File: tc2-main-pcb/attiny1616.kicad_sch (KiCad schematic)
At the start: 21 parts, among them SW101 SW_Push, U117 ATtiny1616-M

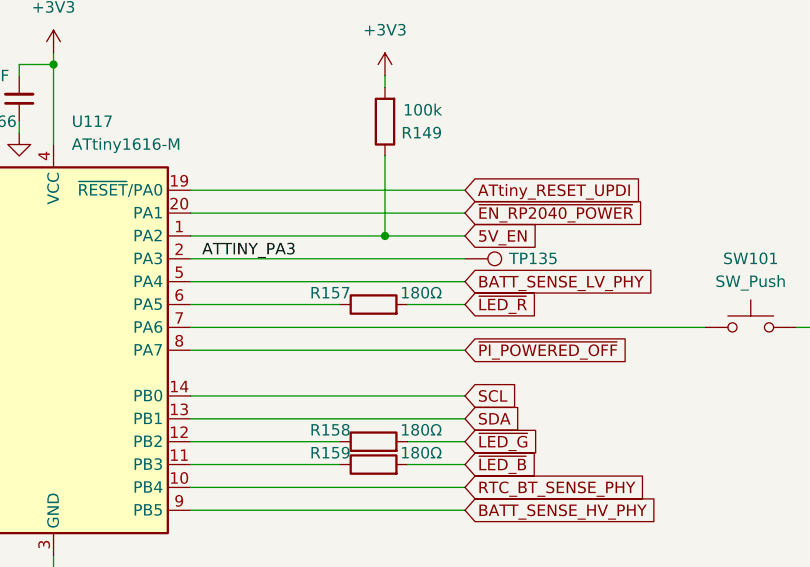
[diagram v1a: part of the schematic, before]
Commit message: Update DC-DC converters
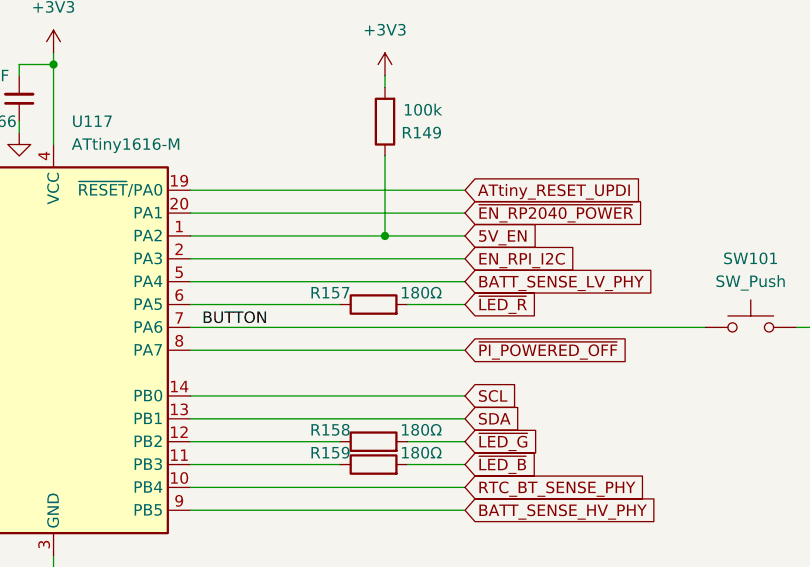
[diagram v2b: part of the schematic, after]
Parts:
- removed TP135: TestPoint, cacophony-library:TP, symbol Connector:TestPoint
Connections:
- net BUTTON: now reaches SW101.1, U117.7 (PA6)
- net ATTINY_PA3 renamed EN_RPI_I2C
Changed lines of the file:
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@@
-		)
-	)
-	(label "ATTINY_PA3"
-		(at 127 109.22 0)
-		(effects
-			(font
-				(size 1.27 1.27)
-			)
-			(justify left bottom)
 		)
 	)
@@
 	(label "EN_PERIPH_POWER_PHY"
 		(at 68.58 129.54 0)
+		(effects
+			(font
+				(size 1.27 1.27)
+			)
+			(justify left bottom)
+		)
+	)
+	(label "BUTTON"
+		(at 127 116.84 0)
 		(effects
 			(font
@@
 				)
 				(justify right)
+			)
+		)
+	)
+	(global_label "EN_RPI_I2C"
+		(shape input)
+		(at 156.21 109.22 0)
+		(fields_autoplaced yes)
+		(effects
+			(font
+				(size 1.27 1.27)
+			)
+			(justify left)
+		)
+		(property "Intersheetrefs" "${INTERSHEET_REFS}"
+			(at 169.1848 109.22 0)
+			(hide yes)
+			(show_name no)
+			(do_not_autoplace no)
+			(effects
+				(font
+					(size 1.27 1.27)
+				)
+				(justify left)
 			)
 		)
@@
 					(unit 1)
 				)
-			)
-		)
-	)
-	(symbol
-		(lib_id "Connector:TestPoint")
-		(at 156.21 109.22 270)
-		(unit 1)
-		(body_style 1)
-		(exclude_from_sim no)
-		(in_bom no)
-		(on_board yes)
-		(in_pos_files yes)
-		(dnp no)
-		(property "Reference" "TP135"
-			(at 163.83 109.22 90)
-			(show_name no)
-			(do_not_autoplace no)
-			(effects
-				(font
-					(size 1.27 1.27)
-				)
-			)
-		)
-		(property "Value" "TestPoint"
-			(at 158.2421 111.76 0)
-			(hide yes)
-			(show_name no)
-			(do_not_autoplace no)
-			(effects
-				(font
-					(size 1.27 1.27)
-				)
-				(justify left)
-			)
-		)
-		(property "Footprint" "cacophony-library:TP"
-			(at 156.21 114.3 0)
-			(hide yes)
-			(show_name no)
-			(do_not_autoplace no)
-			(effects
-				(font
-					(size 1.27 1.27)
-				)
-			)
-		)
-		(property "Datasheet" ""
-			(at 156.21 114.3 0)
-			(hide yes)
-			(show_name no)
-			(do_not_autoplace no)
-			(effects
-				(font
-					(size 1.27 1.27)
-				)
-			)
-		)
-		(property "Description" ""
-			(at 156.21 109.22 0)
-			(hide yes)
-			(show_name no)
-			(do_not_autoplace no)
-			(effects
-				(font
-					(size 1.27 1.27)
-				)
-			)
-		)
-		(pin "1"
-		)
-		(instances
-			(project "tc2-main-pcb"
-				(path "/0662f88c-5300-4b75-bef3-048a3227af84/7647fa78-4fc7-4ed2-904b-b9d3df2998ea"
-					(reference "TP135")
-					(unit 1)
-				)
